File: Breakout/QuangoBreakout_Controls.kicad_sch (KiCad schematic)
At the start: 36 parts, among them J1 Audio_Send_A, J10 Audio_Breakout, J2 Audio_Send_B, J3 Audio_Return_A, J4 Audio_Return_A, J6 Eurorack_10_pin_power, J7 JackMixA, J8 JackMixB, J9 JackMixBoth, U1 TL074

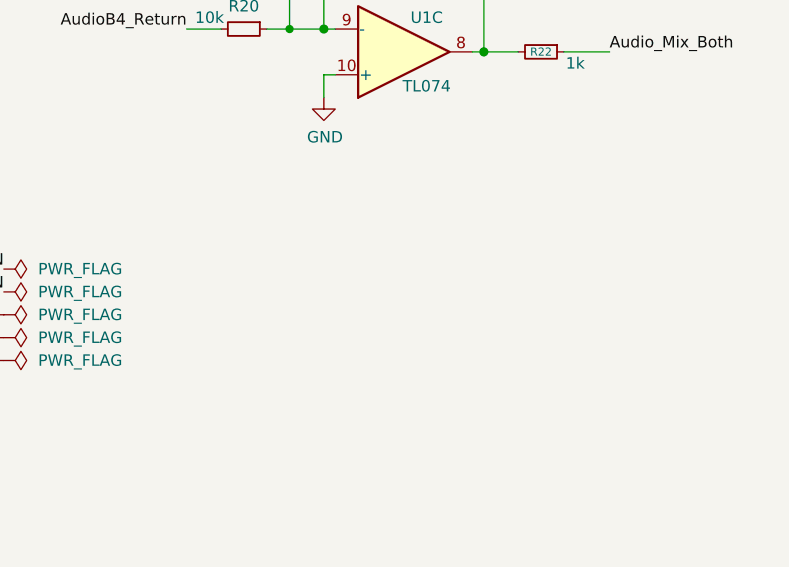
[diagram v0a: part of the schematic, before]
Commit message: Terminated unused op-amp
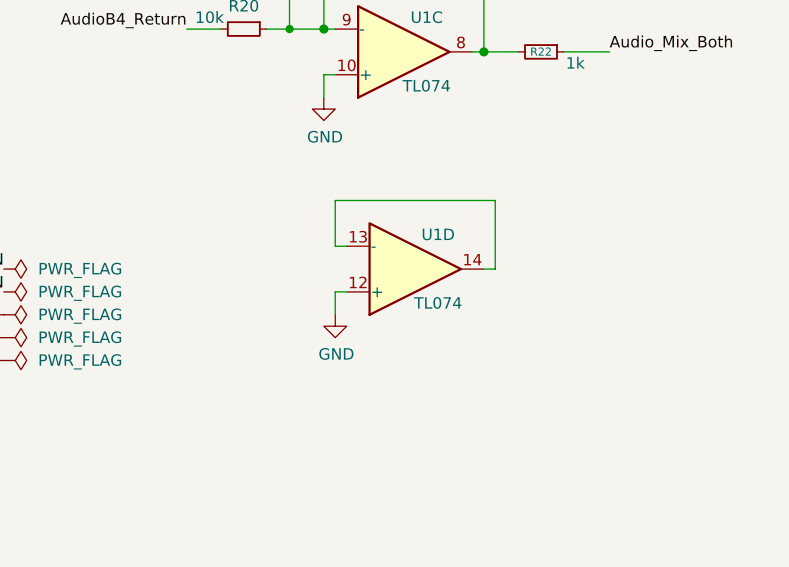
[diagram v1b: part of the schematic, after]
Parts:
- added unit 4 of U1
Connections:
- net GND: now also U1.12 (+)
- new net: U1.13 (-), U1.14

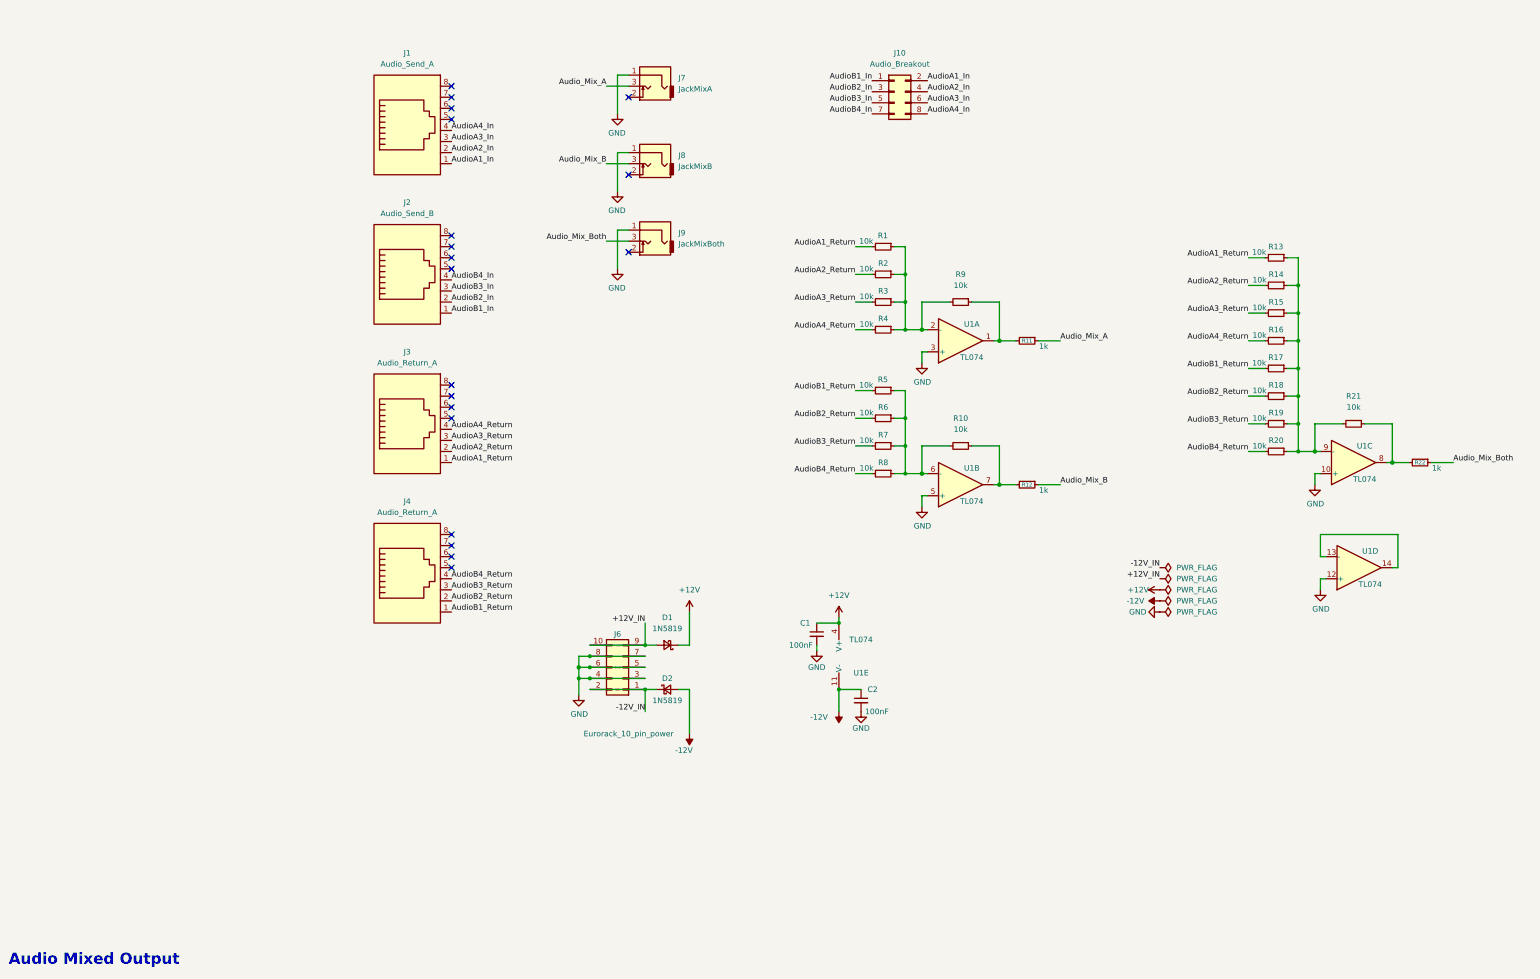
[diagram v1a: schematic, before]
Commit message: Panel labelling
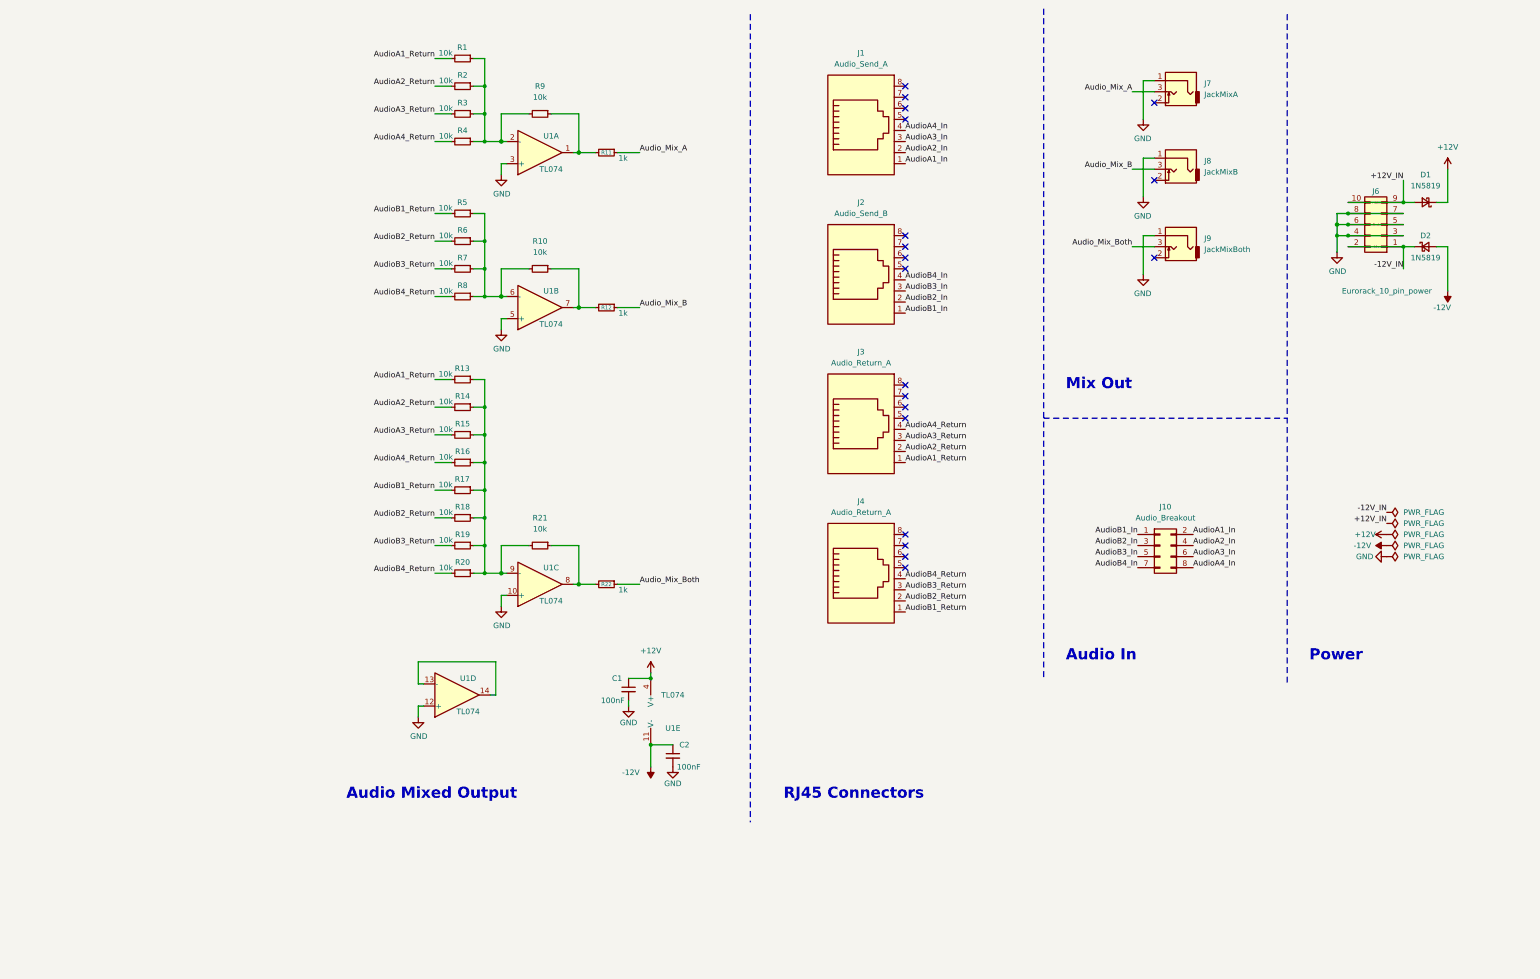
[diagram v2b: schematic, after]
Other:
- note added: "Audio In"
- note added: "Mix Out"
- note added: "Power"
- note added: "RJ45 Connectors"
- title: Quadraphone Controls -> Quango Breakout
- moved on the sheet: C1, C2, D1, D2, J1, J10, J2, J3, J4, J6, J7, J8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

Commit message: Added Readme
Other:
- note added: "v2 fixes: Audio_Mix_A and Audio_Mix_B wrong way round"
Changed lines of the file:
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@@
     (effects (font (size 2.54 2.54) (thickness 0.508) bold) (justify left bottom))
+  )
+  (text "v2 fixes: Audio_Mix_A and Audio_Mix_B wrong way round"
+    (at 182.88 171.45 0)
+    (effects (font (size 1.27 1.27)) (justify left bottom))
   )
   (text "Audio Mixed Output" (at 16.51 193.04 0)
